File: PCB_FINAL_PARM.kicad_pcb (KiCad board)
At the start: 2 copper layers, 87.6 x 95.2 mm, 51 parts, among them J1 Conn_01x02_Servo1, J10 Conn_01x04_TRIS, J11 Conn_01x04_3v3, J2 Conn_01x03_UART1, J3 Conn_01x03_UART2, J4 Conn_01x04_PWM, J5 Conn_01x05_PROGRAMER, J6 Conn_01x02_POWER, J7 Conn_01x02_Servo2, J8 Conn_01x02_Servo3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

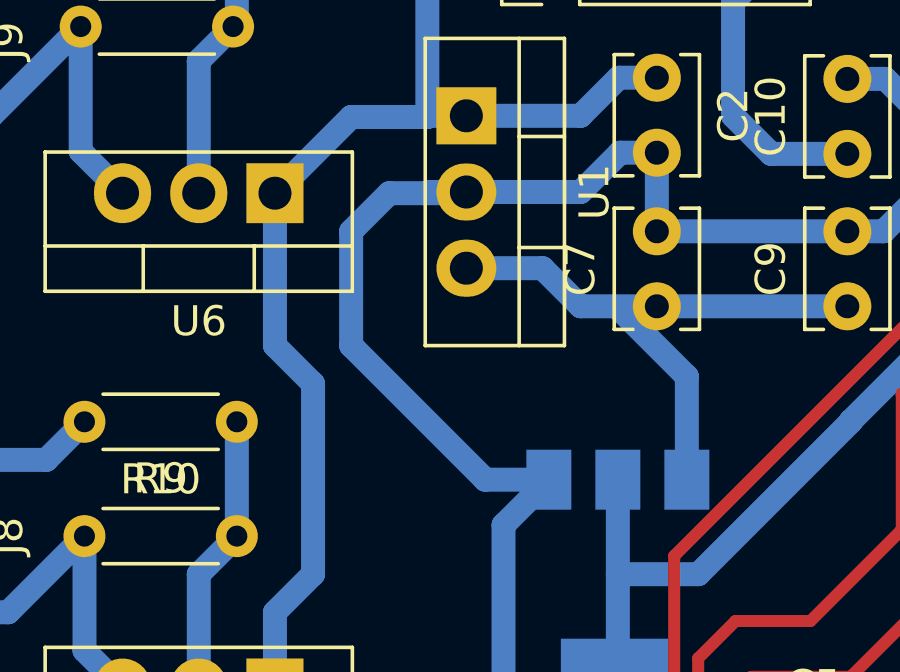
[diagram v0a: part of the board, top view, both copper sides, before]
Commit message: Añadidas las mascaras finales de impresión
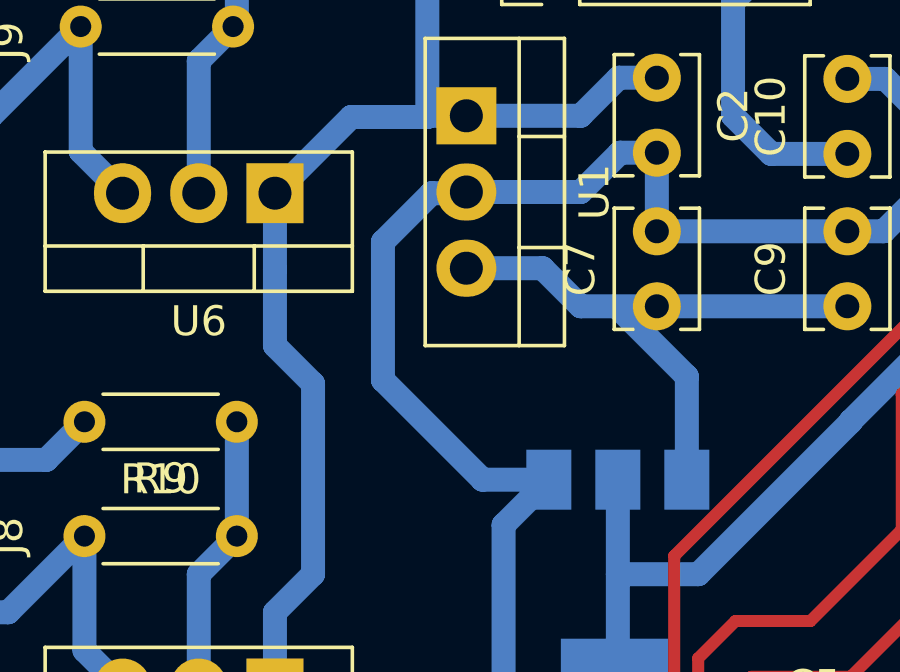
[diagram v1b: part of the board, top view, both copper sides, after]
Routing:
- net GND: track 540.1 -> 537.2 mm

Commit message: Arreglados los LM317
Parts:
- moved R11 5.18 mm to (165.1, 71.8), turned to 180 degrees
- moved R5 5.08 mm to (165.1, 124.5), turned to 180 degrees
- moved R9 5.06 mm to (165.1, 88.8), turned to 180 degrees
- moved R7 5.03 mm to (165.1, 106.5), turned to 180 degrees
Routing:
- net Net-(J7-Pad2): track 14.3 -> 21.7 mm
- net Net-(J8-Pad2): track 14.3 -> 21.3 mm
- net Net-(J9-Pad2): track 14.9 -> 21.8 mm
- net Net-(J1-Pad2): track 14.3 -> 20.7 mm
- net Net-(R11-Pad2): track 9.42 -> 12.6 mm
- net Net-(R7-Pad2): track 9.42 -> 12.4 mm
- net Net-(R10-Pad1): track 9.42 -> 12.4 mm
- net Net-(R5-Pad2): track 9.42 -> 12.2 mm

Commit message: Updated Physical diagram
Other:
- board text added: "+5.4V"
- board text removed: "+6V"
